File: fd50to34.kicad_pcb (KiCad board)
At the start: 2 copper layers, 35.6 x 83.8 mm, 10 parts, among them J1 FD50, J2 FD34

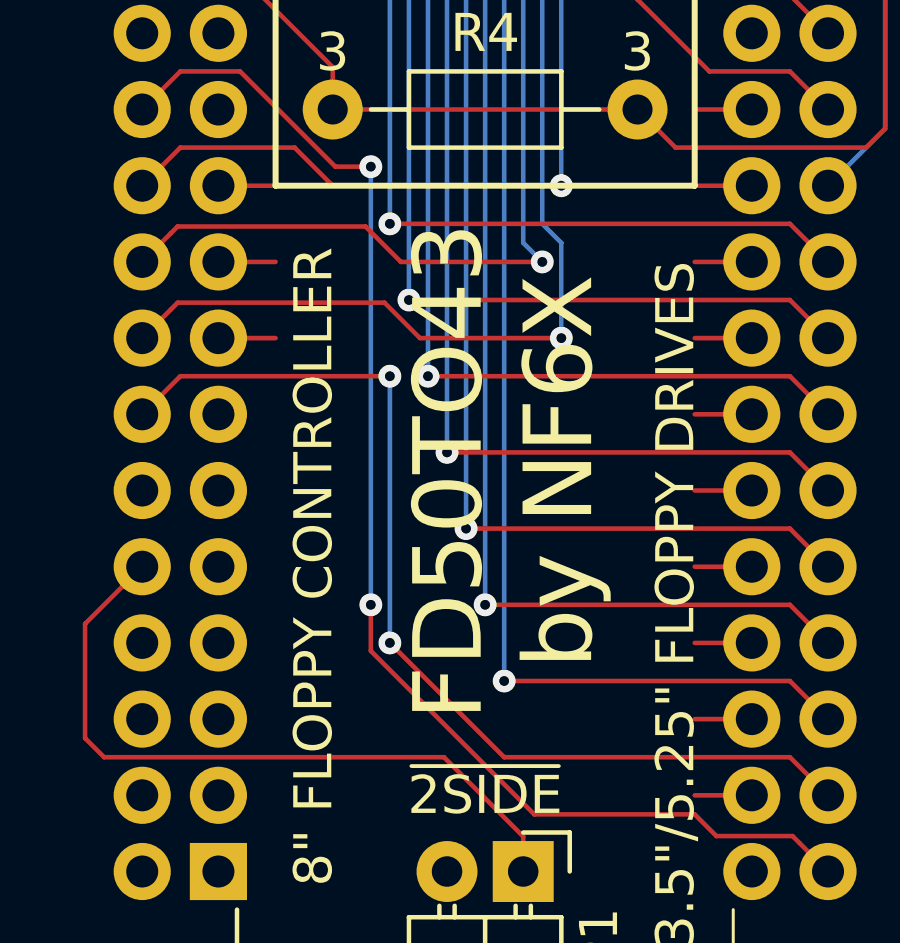
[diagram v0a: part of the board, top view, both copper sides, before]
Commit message: Added errata and changelog file. Corrected top silkscreen typo on PCB. Incremented PCB version to v2. Updated schematic version to 2.0-DRAFT.
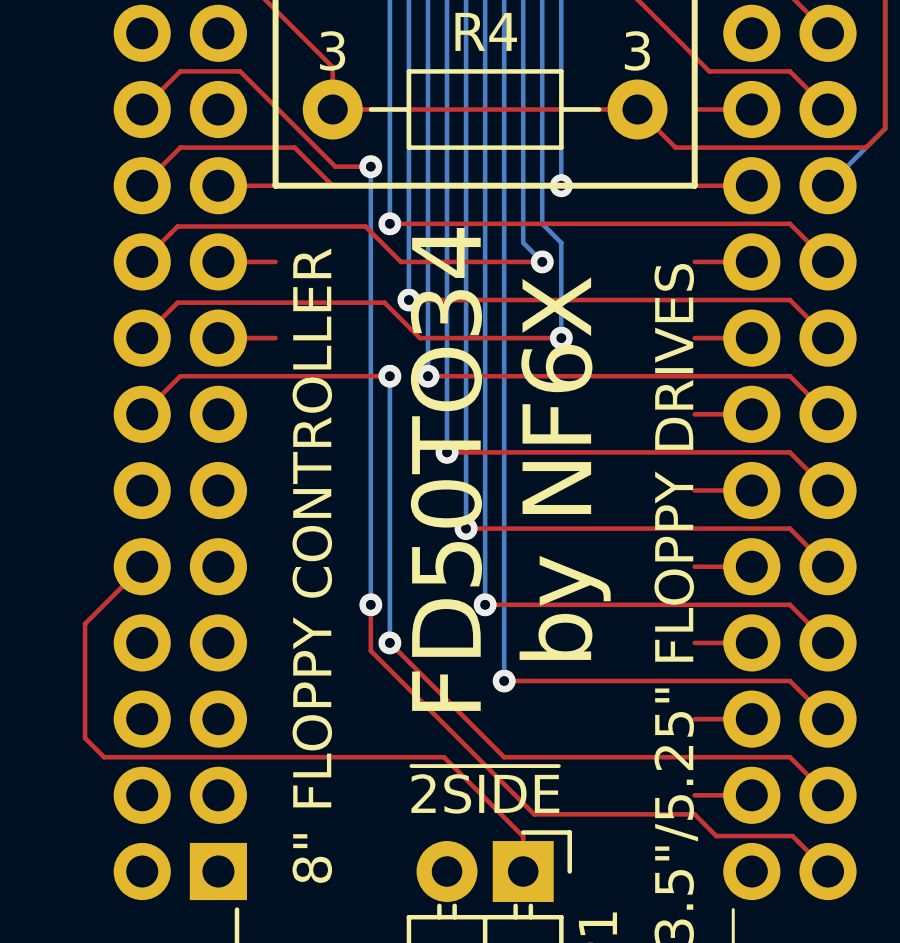
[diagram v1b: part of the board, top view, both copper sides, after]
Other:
- board text added: "FD50TO34 by NF6X"
- board text added: "FD50TO34 v2 by NF6X https://github.com/NF6X/fd50to34"
- board text removed: "FD50TO34 v1 by NF6X https://github.com/NF6X/fd50to34"
- board text removed: "FD50TO43 by NF6X"

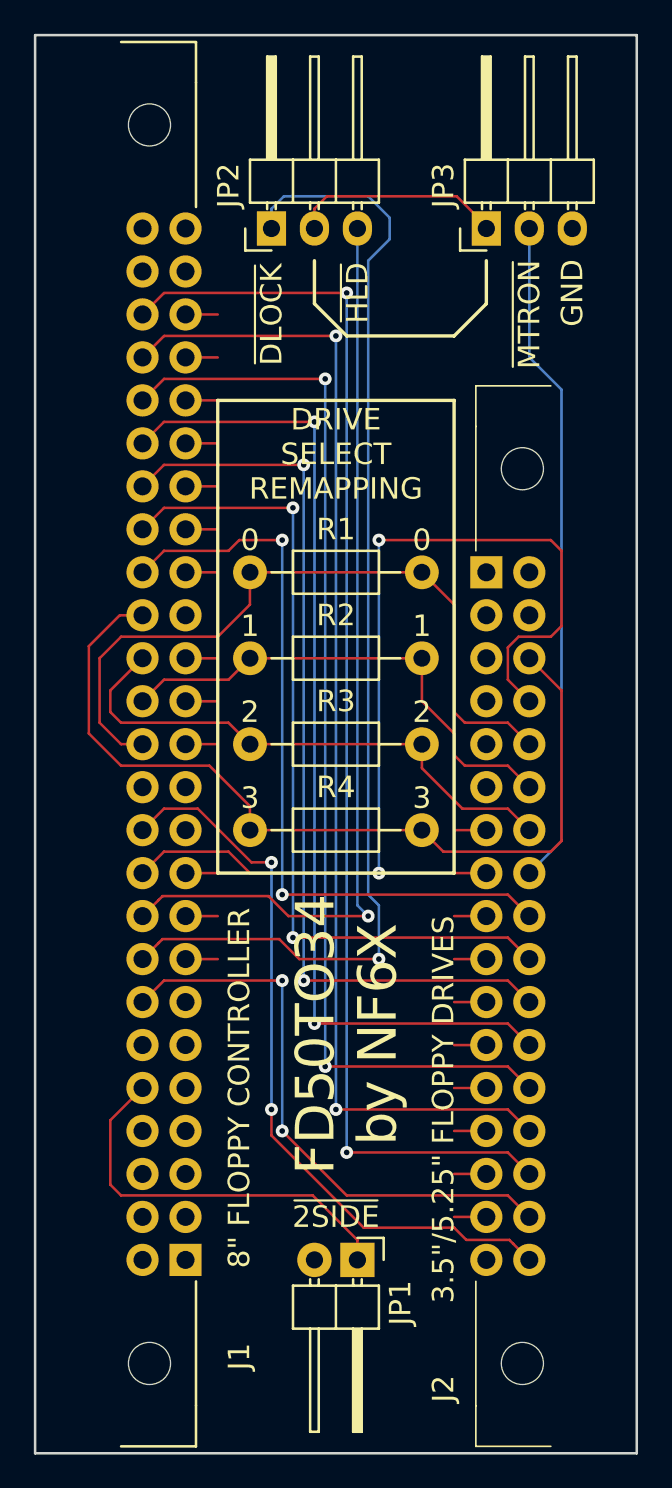
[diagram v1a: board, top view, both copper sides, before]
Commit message: Added density select jumper.
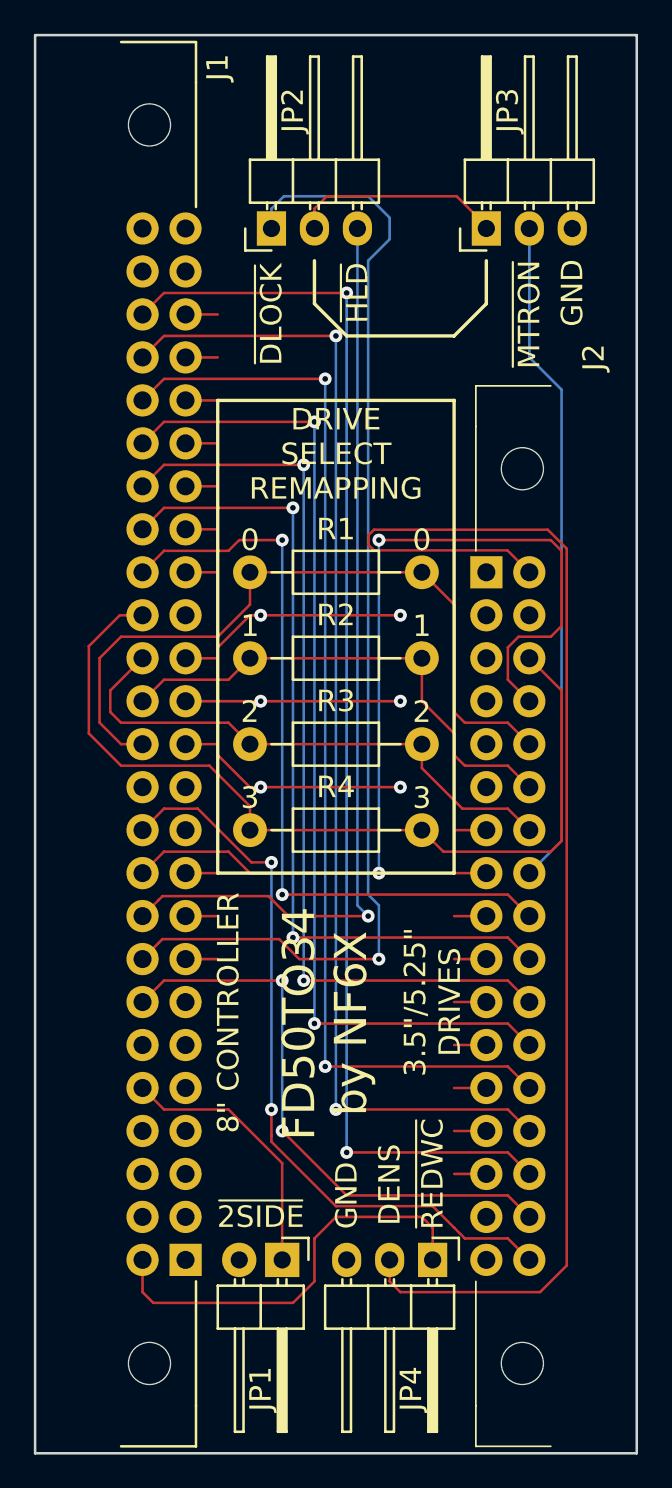
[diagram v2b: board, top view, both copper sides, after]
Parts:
- added JP4: JUMPER3, Pin_Headers:Pin_Header_Angled_1x03, F.Cu at (142.9, 132.1)
- moved JP1 4.44 mm to (134.0, 132.1)
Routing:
- net Net-(J2-Pad2): track 0.00 -> 78.1 mm
- net GND: track 43.8 -> 77.1 mm, vias 0 -> 6
- net Net-(J1-Pad2): track 0.00 -> 25.1 mm
- net Net-(J1-Pad10): track 23.6 -> 15.8 mm
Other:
- board text added: "3.5"/5.25" DRIVES"
- board text added: "8" CONTROLLER"
- board text added: "DENS"
- board text added: "~REDWC"
- board text removed: "3.5"/5.25" FLOPPY DRIVES"
- board text removed: "8" FLOPPY CONTROLLER"

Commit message: Revised part numbers for production quote at MacroFab.
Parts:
- J1: value FD50 -> 61205022121
- J2: value FD34 -> 61203422121
- JP1: value JUMPER -> PBC02SBAN
- JP2, JP3, JP4: value JUMPER3 -> PBC03SBAN
- R1, R2, R3, R4: value 0 -> DNI

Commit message: Removed OSHW logo.
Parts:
- removed G***: OSHW_logo_silkscreen_10mm, NF6X_OSHW_logo:OSHW_logo_silkscreen_10mm
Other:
- board text added: "FD50TO34 v3 by NF6X https://github.com/NF6X/fd50to34"
- board text removed: "FD50TO34 v2 by NF6X https://github.com/NF6X/fd50to34"
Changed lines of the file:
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@@
     (links 73)
     (no_connects 0)
-    (area 119.304999 59.614999 155.015001 143.585001)
+    (area 111.662599 59.614999 164.642206 143.585001)
     (thickness 1.6)
     (drawings 76)
     (tracks 230)
     (zones 0)
-    (modules 11)
+    (modules 10)
     (nets 31)
   )
@@
   (title_block
     (title "fd50to34: Adapt 34 pin floppy drives to 50 pin controllers")
-    (date 2015-07-30)
-    (rev 2)
+    (date 2015-09-22)
+    (rev 3)
     (company "Mark J. Blair <nf6x@nf6x.net>")
     (comment 1 https://github.com/NF6X/fd50to34)
@@
     (0 F.Cu signal)
     (31 B.Cu signal)
-    (36 B.SilkS user hide)
-    (37 F.SilkS user hide)
-    (38 B.Mask user hide)
-    (39 F.Mask user hide)
-    (40 Dwgs.User user hide)
-    (41 Cmts.User user hide)
-    (42 Eco1.User user hide)
-    (43 Eco2.User user hide)
-    (44 Edge.Cuts user hide)
-    (45 Margin user hide)
-    (46 B.CrtYd user hide)
-    (47 F.CrtYd user hide)
-    (48 B.Fab user hide)
-    (49 F.Fab user hide)
+    (36 B.SilkS user)
+    (37 F.SilkS user)
+    (38 B.Mask user)
+    (39 F.Mask user)
+    (40 Dwgs.User user)
+    (41 Cmts.User user)
+    (42 Eco1.User user)
+    (43 Eco2.User user)
+    (44 Edge.Cuts user)
+    (45 Margin user)
+    (46 B.CrtYd user)
+    (47 F.CrtYd user)
+    (48 B.Fab user)
+    (49 F.Fab user)
   )
   (setup
@@
       (net 17 "Net-(J1-Pad32)"))
   )
-  (module NF6X_OSHW_logo:OSHW_logo_silkscreen_10mm (layer B.Cu)
-    (at 145.415 78.74 270)
-    (fp_text reference G*** (at 0 -5.30352 270) (layer B.SilkS) hide
-      (effects (font (size 0.45466 0.45466) (thickness 0.0889)) (justify mirror))
-    )
-    (fp_text value OSHW_logo_silkscreen_10mm (at 0 5.30352 270) (layer B.SilkS) hide
-      (effects (font (size 0.45466 0.45466) (thickness 0.0889)) (justify mirror))
-    )
-    (fp_poly (pts (xy -3.03022 -4.49072) (xy -2.97942 -4.46278) (xy -2.86004 -4.38912) (xy -2.69494 -4.2799)
-      (xy -2.49682 -4.14782) (xy -2.2987 -4.01574) (xy -2.13614 -3.90652) (xy -2.02184 -3.83286)
-      (xy -1.97358 -3.80492) (xy -1.94818 -3.81508) (xy -1.8542 -3.8608) (xy -1.71704 -3.93192)
-      (xy -1.6383 -3.97256) (xy -1.51384 -4.0259) (xy -1.45034 -4.0386) (xy -1.44018 -4.02082)
-      (xy -1.39446 -3.9243) (xy -1.32334 -3.76174) (xy -1.22936 -3.5433) (xy -1.12014 -3.2893)
-      (xy -1.00584 -3.01752) (xy -0.889 -2.73812) (xy -0.77724 -2.47142) (xy -0.68072 -2.23266)
-      (xy -0.60198 -2.03708) (xy -0.55118 -1.90246) (xy -0.53086 -1.84404) (xy -0.53594 -1.83134)
-      (xy -0.59944 -1.77038) (xy -0.70866 -1.6891) (xy -0.94488 -1.49606) (xy -1.17856 -1.20396)
-      (xy -1.3208 -0.87376) (xy -1.36906 -0.50546) (xy -1.32842 -0.1651) (xy -1.1938 0.16256)
-      (xy -0.9652 0.4572) (xy -0.68834 0.67818) (xy -0.36322 0.81534) (xy 0 0.86106)
-      (xy 0.34798 0.82042) (xy 0.68326 0.68834) (xy 0.9779 0.46482) (xy 1.10236 0.32004)
-      (xy 1.27508 0.02286) (xy 1.3716 -0.29718) (xy 1.38176 -0.37846) (xy 1.36906 -0.72898)
-      (xy 1.26492 -1.0668) (xy 1.0795 -1.36906) (xy 0.82042 -1.61544) (xy 0.78994 -1.6383)
-      (xy 0.67056 -1.7272) (xy 0.58928 -1.78816) (xy 0.52832 -1.83896) (xy 0.97536 -2.91592)
-      (xy 1.04648 -3.0861) (xy 1.1684 -3.38074) (xy 1.27762 -3.63474) (xy 1.36144 -3.8354)
-      (xy 1.4224 -3.97002) (xy 1.4478 -4.0259) (xy 1.45034 -4.02844) (xy 1.49098 -4.03606)
-      (xy 1.57226 -4.00558) (xy 1.72212 -3.93192) (xy 1.82118 -3.88112) (xy 1.93548 -3.82524)
-      (xy 1.98882 -3.80492) (xy 2.032 -3.83032) (xy 2.14122 -3.90144) (xy 2.30124 -4.00812)
-      (xy 2.49428 -4.13766) (xy 2.67716 -4.26212) (xy 2.8448 -4.37388) (xy 2.96926 -4.45262)
-      (xy 3.02768 -4.48564) (xy 3.03784 -4.48564) (xy 3.09118 -4.45516) (xy 3.1877 -4.37388)
-      (xy 3.33502 -4.23672) (xy 3.54076 -4.03098) (xy 3.57378 -4.0005) (xy 3.74396 -3.82524)
-      (xy 3.88112 -3.68046) (xy 3.9751 -3.57632) (xy 4.00812 -3.5306) (xy 4.00812 -3.5306)
-      (xy 3.97764 -3.47218) (xy 3.90144 -3.35026) (xy 3.78968 -3.17754) (xy 3.65252 -2.97942)
-      (xy 3.29692 -2.46126) (xy 3.4925 -1.97104) (xy 3.55092 -1.82118) (xy 3.62712 -1.64084)
-      (xy 3.68554 -1.5113) (xy 3.71348 -1.45542) (xy 3.76682 -1.4351) (xy 3.90144 -1.40462)
-      (xy 4.09448 -1.36398) (xy 4.32562 -1.3208) (xy 4.5466 -1.28016) (xy 4.74472 -1.24206)
-      (xy 4.8895 -1.21412) (xy 4.953 -1.20142) (xy 4.96824 -1.19126) (xy 4.98348 -1.16078)
-      (xy 4.9911 -1.0922) (xy 4.99618 -0.97282) (xy 4.99872 -0.78232) (xy 4.99872 -0.50546)
-      (xy 4.99872 -0.47498) (xy 4.99618 -0.21336) (xy 4.9911 -0.00254) (xy 4.98348 0.13462)
-      (xy 4.97586 0.18796) (xy 4.97332 0.18796) (xy 4.91236 0.2032) (xy 4.77266 0.23368)
-      (xy 4.572 0.27178) (xy 4.33578 0.3175) (xy 4.32054 0.32004) (xy 4.08432 0.36576)
-      (xy 3.8862 0.4064) (xy 3.7465 0.43942) (xy 3.68808 0.4572) (xy 3.67538 0.47498)
-      (xy 3.62966 0.56642) (xy 3.56108 0.71374) (xy 3.48234 0.89154) (xy 3.40614 1.07696)
-      (xy 3.33756 1.2446) (xy 3.29438 1.36906) (xy 3.27914 1.42494) (xy 3.28168 1.42748)
-      (xy 3.31724 1.48336) (xy 3.39852 1.60528) (xy 3.51282 1.77546) (xy 3.64998 1.97866)
-      (xy 3.66014 1.9939) (xy 3.7973 2.19202) (xy 3.90652 2.3622) (xy 3.98018 2.48158)
-      (xy 4.00812 2.53746) (xy 4.00812 2.54) (xy 3.9624 2.60096) (xy 3.8608 2.71272)
-      (xy 3.71602 2.86512) (xy 3.54076 3.04292) (xy 3.48488 3.09626) (xy 3.2893 3.28676)
-      (xy 3.15468 3.41122) (xy 3.07086 3.47726) (xy 3.03022 3.4925) (xy 3.03022 3.48996)
-      (xy 2.96926 3.4544) (xy 2.84226 3.37312) (xy 2.67208 3.25628) (xy 2.46888 3.11912)
-      (xy 2.45364 3.10896) (xy 2.25552 2.9718) (xy 2.08788 2.86004) (xy 1.97104 2.7813)
-      (xy 1.9177 2.75082) (xy 1.91008 2.75082) (xy 1.8288 2.77368) (xy 1.68656 2.82448)
-      (xy 1.5113 2.89306) (xy 1.32588 2.96672) (xy 1.15824 3.03784) (xy 1.03124 3.09372)
-      (xy 0.97282 3.12928) (xy 0.97028 3.13182) (xy 0.94996 3.20294) (xy 0.9144 3.3528)
-      (xy 0.87376 3.55854) (xy 0.8255 3.80238) (xy 0.81788 3.84302) (xy 0.7747 4.08178)
-      (xy 0.7366 4.27736) (xy 0.70866 4.41452) (xy 0.69342 4.4704) (xy 0.6604 4.47802)
-      (xy 0.54356 4.48564) (xy 0.36576 4.49072) (xy 0.14986 4.49326) (xy -0.0762 4.49072)
-      (xy -0.29718 4.48564) (xy -0.48514 4.48056) (xy -0.61976 4.4704) (xy -0.67564 4.46024)
-      (xy -0.67818 4.45516) (xy -0.6985 4.3815) (xy -0.73152 4.23164) (xy -0.7747 4.0259)
-      (xy -0.82042 3.77952) (xy -0.83058 3.73634) (xy -0.87376 3.50012) (xy -0.9144 3.30454)
-      (xy -0.94234 3.16992) (xy -0.95758 3.11658) (xy -0.98044 3.10642) (xy -1.07696 3.06324)
-      (xy -1.23698 2.9972) (xy -1.4351 2.91846) (xy -1.8923 2.73304) (xy -2.45364 3.11658)
-      (xy -2.50444 3.15214) (xy -2.70764 3.2893) (xy -2.87274 3.39852) (xy -2.98704 3.47472)
-      (xy -3.0353 3.50012) (xy -3.04038 3.50012) (xy -3.09626 3.44932) (xy -3.20548 3.34518)
-      (xy -3.35788 3.19786) (xy -3.53568 3.0226) (xy -3.66522 2.89052) (xy -3.82016 2.73304)
-      (xy -3.91922 2.6289) (xy -3.97256 2.56032) (xy -3.99034 2.51968) (xy -3.98526 2.49174)
-      (xy -3.9497 2.43332) (xy -3.86842 2.3114) (xy -3.75158 2.14122) (xy -3.61442 1.9431)
-      (xy -3.50266 1.77546) (xy -3.38074 1.5875) (xy -3.302 1.45288) (xy -3.27406 1.38684)
-      (xy -3.28168 1.36144) (xy -3.31978 1.24968) (xy -3.38836 1.08458) (xy -3.47218 0.88646)
-      (xy -3.66776 0.44196) (xy -3.95732 0.38608) (xy -4.13512 0.35306) (xy -4.3815 0.3048)
-      (xy -4.61772 0.25908) (xy -4.98602 0.18796) (xy -4.99872 -1.16586) (xy -4.94284 -1.19126)
-      (xy -4.88696 -1.2065) (xy -4.7498 -1.23698) (xy -4.55676 -1.27508) (xy -4.32562 -1.31826)
-      (xy -4.13004 -1.35382) (xy -3.93192 -1.39192) (xy -3.78968 -1.41986) (xy -3.72872 -1.43256)
-      (xy -3.71094 -1.45542) (xy -3.66268 -1.5494) (xy -3.59156 -1.7018) (xy -3.51282 -1.88468)
-      (xy -3.43408 -2.07518) (xy -3.3655 -2.25044) (xy -3.31724 -2.38252) (xy -3.29692 -2.4511)
-      (xy -3.32486 -2.50444) (xy -3.39852 -2.62128) (xy -3.50774 -2.78638) (xy -3.64236 -2.98196)
-      (xy -3.77698 -3.17754) (xy -3.89128 -3.34518) (xy -3.97002 -3.4671) (xy -4.00304 -3.52298)
-      (xy -3.98526 -3.55854) (xy -3.90652 -3.65506) (xy -3.7592 -3.80746) (xy -3.53822 -4.0259)
-      (xy -3.50266 -4.06146) (xy -3.3274 -4.2291) (xy -3.18008 -4.36626) (xy -3.07594 -4.4577)
-      (xy -3.03022 -4.49072)) (layer B.SilkS) (width 0.00254))
-  )
   (module Pin_Headers:Pin_Header_Angled_1x03 (layer F.Cu)
     (at 142.875 132.08 270)
@@
     (effects (font (size 1.27 1.27) (thickness 0.127)) (justify mirror))
   )
-  (gr_text "FD50TO34 v2 by NF6X\nhttps://github.com/NF6X/fd50to34" (at 137.16 101.6 90) (layer B.SilkS)
+  (gr_text "FD50TO34 v3 by NF6X\nhttps://github.com/NF6X/fd50to34" (at 137.16 101.6 90) (layer B.SilkS)
     (effects (font (size 1.905 1.905) (thickness 0.1905)) (justify mirror))
   )
